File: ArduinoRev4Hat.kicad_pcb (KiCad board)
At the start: 2 copper layers, 52.5 x 97.5 mm, 11 parts, among them J1 Conn_01x10_Pin, J10 73099-0, J11 73099-0, J2 Conn_01x08_Pin, J3 Conn_01x04_Pin, J4 Conn_01x04_Pin, J5 Conn_01x04_Pin, J7 73099-0, J8 73099-0, J9 73099-0

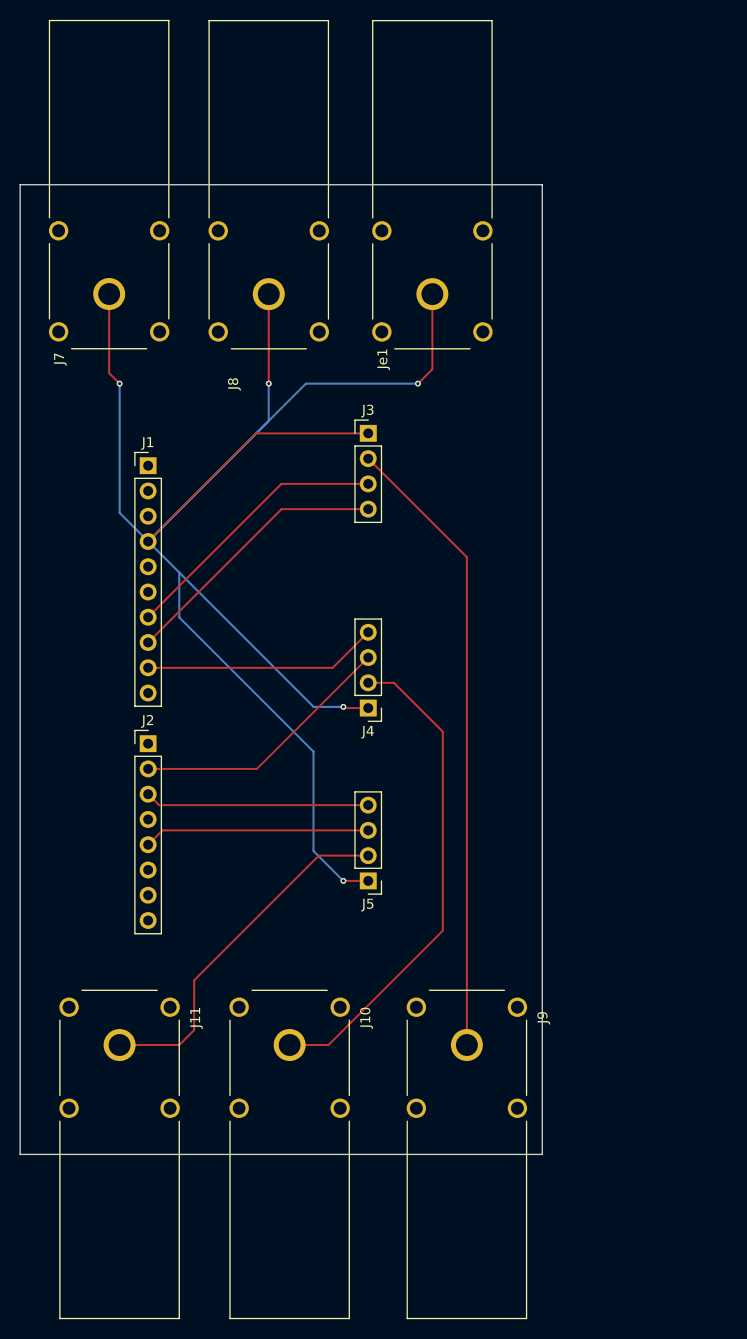
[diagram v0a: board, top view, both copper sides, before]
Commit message: Added a ground plane to the PCB plus added .gitignore
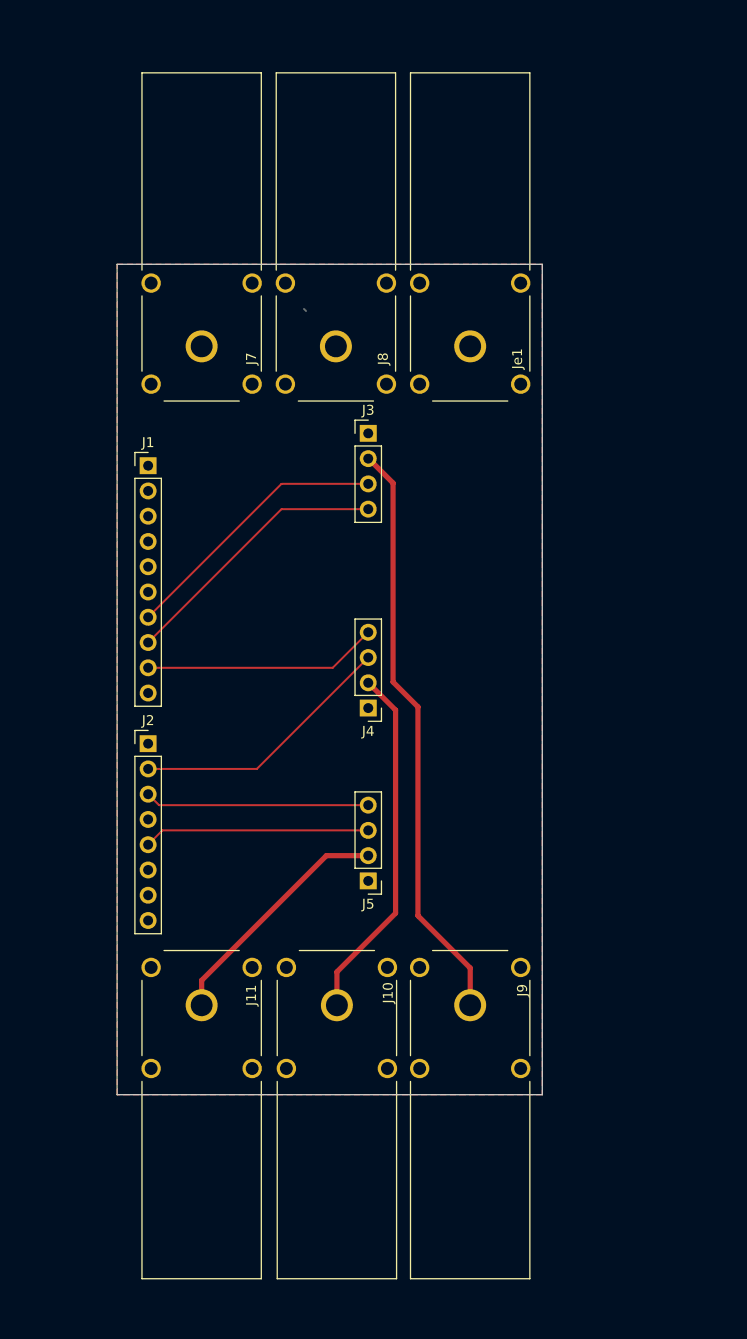
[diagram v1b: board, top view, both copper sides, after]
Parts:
- moved J7 10.7 mm to (75.8, 63.8)
- moved J11 9.17 mm to (75.8, 130.0)
- moved J8 8.55 mm to (89.2, 63.8)
- moved Je1 6.48 mm to (102.8, 63.8)
- moved J10 6.21 mm to (89.3, 130.0)
- moved J9 4.01 mm to (102.8, 130.0)
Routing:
- net GND: track 195.7 -> 0.27 mm, vias 5 -> 0
- net /VM: track 148.6 -> 119.7 mm
- added copper zone on F.Cu, net GND
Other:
- board size 52.5 x 97.5 mm -> 42.8 x 83.5 mm

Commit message: updated the layout of the pcb; added logo and credits; investaged potential components for the print
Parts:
- added G***: LOGO, IrishSat_Logo:IrishSat-Logo, F.Cu at (98.5, 83.0)
- H-Bridge 1: renamed from J3
- H-Bridge 2: renamed from J4
- H-Bridge 3: renamed from J5
- moved H-Bridge 1 7.50 mm to (85.0, 72.5)
- moved H-Bridge 2 7.50 mm to (85.0, 100.1)
- moved H-Bridge 3 7.50 mm to (85.0, 117.5)
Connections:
- net Net-(J1-Pin_7) renamed /IN1_X
- net Net-(J1-Pin_8) renamed /IN2_X
- net Net-(J1-Pin_9) renamed /IN2_Y
- net Net-(J2-Pin_2) renamed /IN1_Y
- net Net-(J2-Pin_3) renamed /IN2_Z
- net Net-(J2-Pin_5) renamed /IN1_Z
- H-Bridge 1 pad 2: /VM -> /VM_X
- H-Bridge 2 pad 2: /VM -> /VM_Y
- H-Bridge 3 pad 2: /VM -> /VM_Z
- J10 pad 1: /VM -> /VM_Y
- J11 pad 1: /VM -> /VM_Z
- J9 pad 1: /VM -> /VM_X
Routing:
- net /VM: track 119.7 -> 0.00 mm
- net /VM_X: track 0.00 -> 67.7 mm
- net /VM_Y: track 0.00 -> 34.2 mm
- net /VM_Z: track 0.00 -> 26.8 mm
- net /IN2_Z: track 22.6 -> 15.1 mm
- net /IN1_Z: track 22.7 -> 15.2 mm
- net /IN2_Y: track 23.6 -> 16.1 mm
- net /IN1_Y: track 26.8 -> 24.7 mm
- net /IN1_X: track 27.7 -> 29.7 mm
- net /IN2_X: track 27.7 -> 26.0 mm
- added copper zone on B.Cu, net GND
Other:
- board text added: "Goat Lab Arduino Hat by Andres Perez (28')"

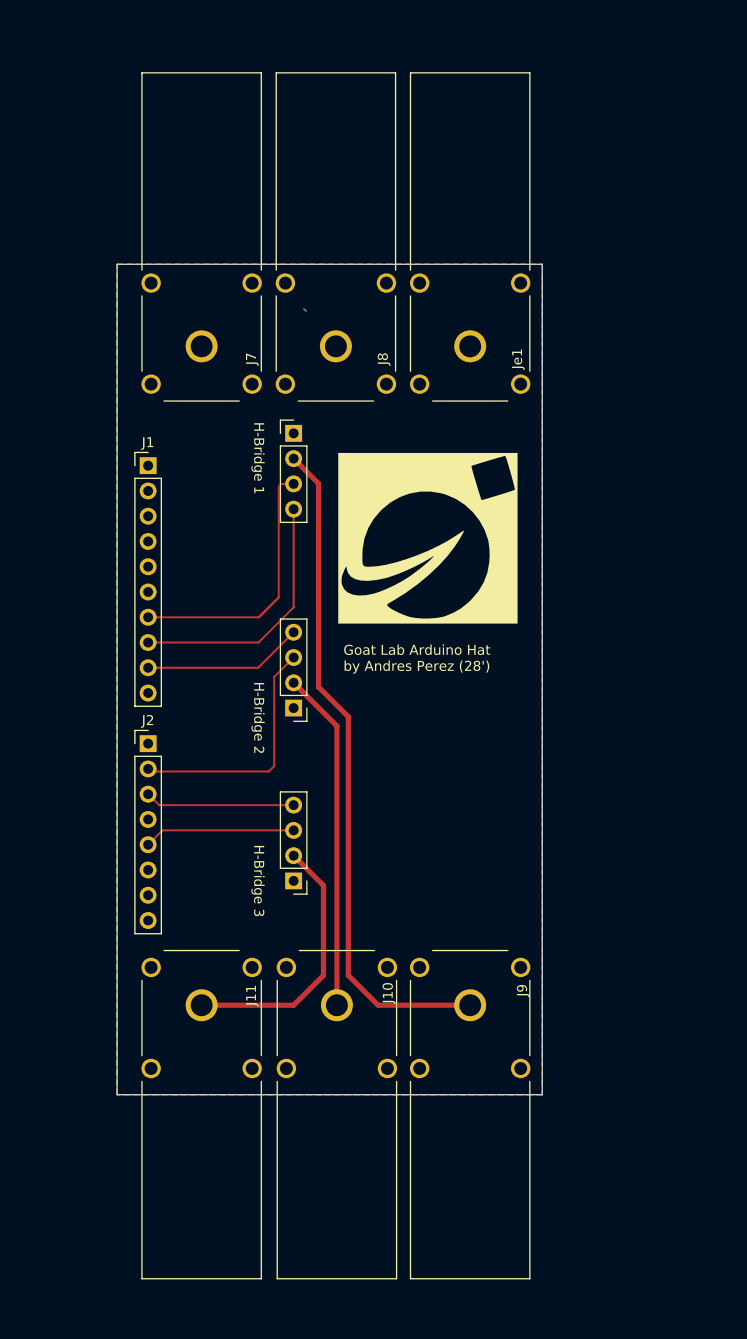
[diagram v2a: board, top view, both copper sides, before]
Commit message: changed logo; moved banana plugs location; swaped in1_x and in2_x pin for a better layout;
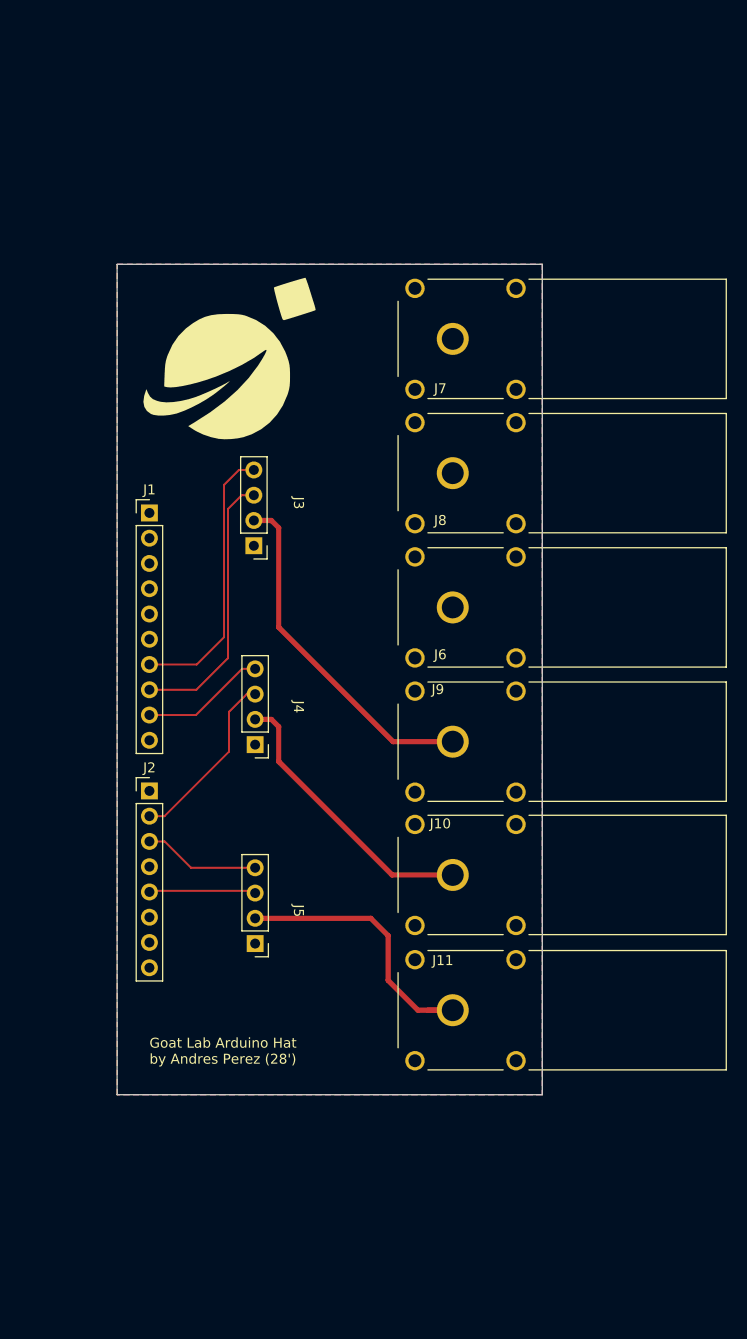
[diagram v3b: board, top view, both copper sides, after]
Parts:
- removed the G*** at (98.5, 83.0)
- added G***: LOGO, IrishSat_Logo:IrishSat-Logo-inverted, F.Cu at (78.5, 65.0)
- J3: renamed from H-Bridge 1
- J4: renamed from H-Bridge 2
- J5: renamed from H-Bridge 3
- moved J9 26.6 mm to (101.0, 103.5), turned to 0 degrees
- moved J6 26.3 mm to (101.0, 90.0), turned to 0 degrees
- moved J7 25.3 mm to (101.0, 63.0), turned to 0 degrees
- moved J11 25.3 mm to (101.0, 130.5), turned to 0 degrees
- moved J10 17.5 mm to (101.0, 116.9), turned to 0 degrees
- moved J8 17.3 mm to (101.0, 76.5), turned to 0 degrees
- moved J3 12.0 mm to (81.0, 83.8), turned to 180 degrees
- moved J5 7.39 mm to (81.1, 123.8)
- moved J4 5.34 mm to (81.1, 103.8)
- moved J1 4.75 mm to (70.5, 80.5)
- moved J2 4.75 mm to (70.5, 108.5)
- renumbered Je1 to J6
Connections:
- J1 pad 7: /IN1_X -> /IN2_X
- J1 pad 8: /IN2_X -> /IN1_X
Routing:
- net /VM_X: track 67.7 -> 35.1 mm
- net /IN1_Y: track 24.7 -> 18.1 mm
- net /VM_Y: track 34.2 -> 28.4 mm
- net /IN1_Z: track 15.2 -> 10.8 mm
- net /IN2_Y: track 16.1 -> 12.6 mm
- net /IN2_Z: track 15.1 -> 11.7 mm
- net /IN1_X: track 29.7 -> 27.4 mm
- net /IN2_X: track 26.0 -> 28.1 mm
- net /VM_Z: track 26.8 -> 28.8 mm
